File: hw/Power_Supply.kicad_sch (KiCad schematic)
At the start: 16 parts, among them U1 XC6206P332MR, U2 XC6206P332MR

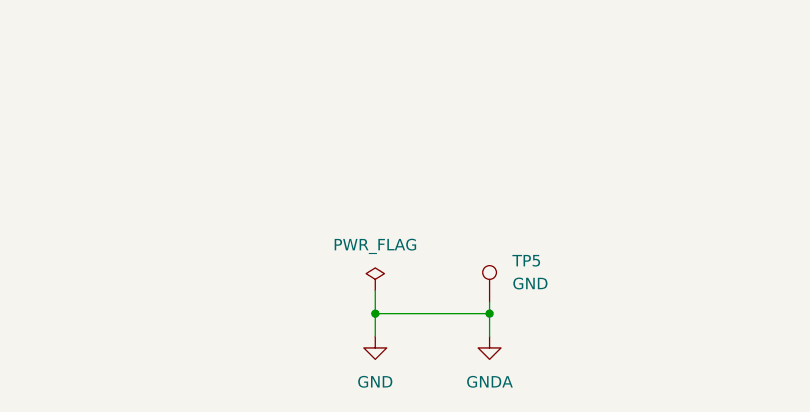
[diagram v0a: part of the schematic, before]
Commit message: added new pcb design, ERC errors not fixed yet
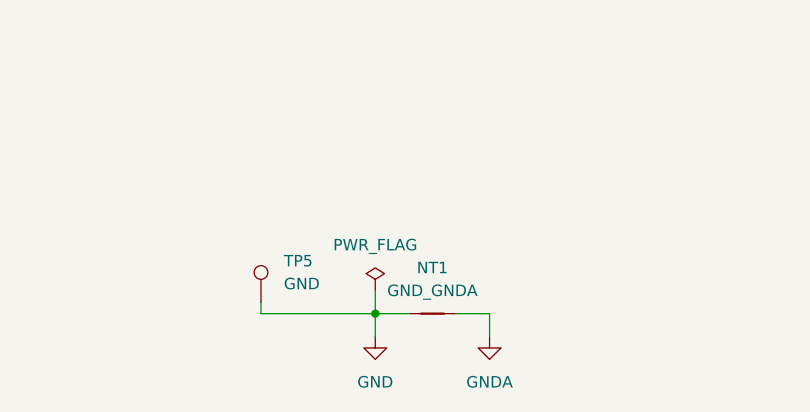
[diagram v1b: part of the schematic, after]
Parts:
- added NT1: GND_GNDA, NetTie:NetTie-2_SMD_Pad0.5mm, symbol Device:NetTie_2
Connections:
- net GND: now also NT1.1; no longer C6.2, C7.2, C8.2, U2.1 (GND)
- new net GNDA: C6.2, C7.2, C8.2, NT1.2, U2.1 (GND)
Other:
- moved on the sheet: TP5

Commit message: updates to hardware layer
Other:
- moved on the sheet: NT1, TP5
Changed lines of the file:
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@@
 	)
 	(junction
-		(at 149.86 176.53)
+		(at 83.82 163.83)
 		(diameter 0)
 		(color 0 0 0 0)
@@
 		(color 0 0 0 0)
 	)
+	(junction
+		(at 96.52 163.83)
+		(diameter 0)
+		(color 0 0 0 0)
+	)
 	(wire
 		(pts
@@
 	(wire
 		(pts
+			(xy 81.28 163.83) (xy 83.82 163.83)
+		)
+		(stroke
+			(width 0)
+			(type default)
+		)
+	)
+	(wire
+		(pts
 			(xy 203.2 91.44) (xy 203.2 88.9)
 		)
@@
 	(wire
 		(pts
-			(xy 149.86 173.99) (xy 149.86 176.53)
-		)
-		(stroke
-			(width 0)
-			(type default)
-		)
-	)
-	(wire
-		(pts
 			(xy 74.93 81.28) (xy 77.47 81.28)
 		)
@@
 	(wire
 		(pts
-			(xy 149.86 176.53) (xy 153.67 176.53)
+			(xy 83.82 163.83) (xy 87.63 163.83)
 		)
 		(stroke
@@
 	(wire
 		(pts
-			(xy 137.16 175.26) (xy 137.16 176.53)
+			(xy 83.82 162.56) (xy 83.82 163.83)
 		)
 		(stroke
@@
 	(wire
 		(pts
-			(xy 149.86 176.53) (xy 149.86 179.07)
+			(xy 83.82 163.83) (xy 83.82 166.37)
 		)
 		(stroke
@@
 	(wire
 		(pts
-			(xy 137.16 176.53) (xy 149.86 176.53)
-		)
-		(stroke
-			(width 0)
-			(type default)
-		)
-	)
-	(wire
-		(pts
 			(xy 135.89 101.6) (xy 148.59 101.6)
 		)
@@
 	(wire
 		(pts
+			(xy 99.06 163.83) (xy 96.52 163.83)
+		)
+		(stroke
+			(width 0)
+			(type default)
+		)
+	)
+	(wire
+		(pts
 			(xy 135.89 86.36) (xy 135.89 88.9)
 		)
@@
 	(wire
 		(pts
-			(xy 158.75 176.53) (xy 162.56 176.53)
+			(xy 92.71 163.83) (xy 96.52 163.83)
 		)
 		(stroke
@@
 	(wire
 		(pts
-			(xy 162.56 176.53) (xy 162.56 179.07)
+			(xy 96.52 163.83) (xy 96.52 166.37)
 		)
 		(stroke
@@
 	(symbol
 		(lib_id "power:PWR_FLAG")
-		(at 149.86 173.99 0)
-		(mirror y)
+		(at 99.06 163.83 270)
+		(mirror x)
+		(unit 1)
+		(exclude_from_sim no)
+		(in_bom yes)
+		(on_board yes)
+		(dnp no)
+		(fields_autoplaced yes)
+		(property "Reference" "#FLG01"
+			(at 100.965 163.83 0)
+			(effects
+				(font
+					(size 1.27 1.27)
+				)
+				(hide yes)
+			)
+		)
+		(property "Value" "PWR_FLAG"
+			(at 102.87 163.8299 90)
+			(effects
+				(font
+					(size 1.27 1.27)
+				)
+				(justify left)
+			)
+		)
+		(property "Footprint" ""
+			(at 99.06 163.83 0)
+			(effects
+				(font
+					(size 1.27 1.27)
+				)
+				(hide yes)
+			)
+		)
+		(property "Datasheet" "~"
+			(at 99.06 163.83 0)
+			(effects
+				(font
+					(size 1.27 1.27)
+				)
+				(hide yes)
+			)
+		)
+		(property "Description" "Special symbol for telling ERC where power comes from"
+			(at 99.06 163.83 0)
+			(effects
+				(font
+					(size 1.27 1.27)
+				)
+				(hide yes)
+			)
+		)
+		(pin "1"
+		)
+		(instances
+			(project "Expresso"
+				(path "/1e7cbae1-0003-4e27-ba62-2dd55b10f4f2/7b3e7736-e5d0-49f7-ac58-655fac733912"
+					(reference "#FLG01")
+					(unit 1)
+				)
+			)
+		)
+	)
+	(symbol
+		(lib_id "power:PWR_FLAG")
+		(at 81.28 163.83 90)
+		(mirror x)
 		(unit 1)
 		(exclude_from_sim no)
@@
 		(fields_autoplaced yes)
 		(property "Reference" "#FLG0101"
-			(at 149.86 172.085 0)
+			(at 79.375 163.83 0)
 			(effects
 				(font
@@
 		)
 		(property "Value" "PWR_FLAG"
-			(at 149.86 168.91 0)
-			(effects
-				(font
-					(size 1.27 1.27)
-				)
+			(at 77.47 163.8299 90)
+			(effects
+				(font
+					(size 1.27 1.27)
+				)
+				(justify left)
 			)
 		)
 		(property "Footprint" ""
-			(at 149.86 173.99 0)
+			(at 81.28 163.83 0)
 			(effects
 				(font
@@
 		)
 		(property "Datasheet" "~"
-			(at 149.86 173.99 0)
+			(at 81.28 163.83 0)
 			(effects
 				(font
@@
 		)
 		(property "Description" "Special symbol for telling ERC where power comes from"
-			(at 149.86 173.99 0)
+			(at 81.28 163.83 0)
 			(effects
 				(font
@@
 	(symbol
 		(lib_id "Connector:TestPoint")
-		(at 137.16 175.26 0)
+		(at 83.82 162.56 0)
 		(unit 1)
 		(exclude_from_sim no)
@@
 		(fields_autoplaced yes)
 		(property "Reference" "TP5"
-			(at 139.7 170.6879 0)
-			(effects
-				(font
-					(size 1.27 1.27)
-				)
-				(justify left)
+			(at 83.82 153.67 0)
+			(effects
+				(font
+					(size 1.27 1.27)
+				)
 			)
 		)
 		(property "Value" "GND"
-			(at 139.7 173.2279 0)
-			(effects
-				(font
-					(size 1.27 1.27)
-				)
-				(justify left)
+			(at 83.82 156.21 0)
+			(effects
+				(font
+					(size 1.27 1.27)
+				)
 			)
 		)
 		(property "Footprint" "TestPoint:TestPoint_Pad_D2.0mm"
-			(at 142.24 175.26 0)
+			(at 88.9 162.56 0)
 			(effects
 				(font
@@
 		)
 		(property "Datasheet" "~"
-			(at 142.24 175.26 0)
+			(at 88.9 162.56 0)
 			(effects
 				(font
@@
 		)
 		(property "Description" "test point"
-			(at 137.16 175.26 0)
+			(at 83.82 162.56 0)
 			(effects
 				(font
@@
 	(symbol
 		(lib_id "power:GND")
-		(at 149.86 179.07 0)
+		(at 83.82 166.37 0)
 		(unit 1)
 		(exclude_from_sim no)
@@
 		(fields_autoplaced yes)
 		(property "Reference" "#PWR0101"
-			(at 149.86 185.42 0)
+			(at 83.82 172.72 0)
 			(effects
 				(font
@@
 		)
 		(property "Value" "GND"
-			(at 149.86 184.15 0)
+			(at 83.82 171.45 0)
 			(effects
 				(font
@@
 		)
 		(property "Footprint" ""
-			(at 149.86 179.07 0)
+			(at 83.82 166.37 0)
 			(effects
 				(font
@@
 		)
 		(property "Datasheet" ""
-			(at 149.86 179.07 0)
+			(at 83.82 166.37 0)
 			(effects
 				(font
@@
 		)
 		(property "Description" "Power symbol creates a global label with name \"GND\" , ground"
-			(at 149.86 179.07 0)
+			(at 83.82 166.37 0)
 			(effects
 				(font
@@
 	(symbol
 		(lib_id "power:GNDA")
-		(at 162.56 179.07 0)
+		(at 96.52 166.37 0)
 		(unit 1)
 		(exclude_from_sim no)
@@
 		(fields_autoplaced yes)
 		(property "Reference" "#PWR0102"
-			(at 162.56 185.42 0)
+			(at 96.52 172.72 0)
 			(effects
 				(font
@@
 		)
 		(property "Value" "GNDA"
-			(at 162.56 184.15 0)
+			(at 96.52 171.45 0)
 			(effects
 				(font
@@
 		)
 		(property "Footprint" ""
-			(at 162.56 179.07 0)
+			(at 96.52 166.37 0)
 			(effects
 				(font
@@
 		)
 		(property "Datasheet" ""
-			(at 162.56 179.07 0)
+			(at 96.52 166.37 0)
 			(effects
 				(font
@@
 		)
 		(property "Description" "Power symbol creates a global label with name \"GNDA\" , analog ground"
-			(at 162.56 179.07 0)
+			(at 96.52 166.37 0)
 			(effects
 				(font
@@
 	(symbol
 		(lib_id "Device:NetTie_2")
-		(at 156.21 176.53 0)
+		(at 90.17 163.83 0)
 		(unit 1)
 		(exclude_from_sim no)
@@
 		(dnp no)
 		(property "Reference" "NT1"
-			(at 156.21 171.45 0)
+			(at 90.17 158.75 0)
 			(effects
 				(font
@@
 		)
 		(property "Value" "GND_GNDA"
-			(at 156.21 173.99 0)
+			(at 90.17 161.29 0)
 			(effects
 				(font
@@
 		)
 		(property "Footprint" "NetTie:NetTie-2_SMD_Pad0.5mm"
-			(at 156.21 176.53 0)
+			(at 90.17 163.83 0)
 			(effects
 				(font
@@
 		)
 		(property "Datasheet" "~"
-			(at 156.21 176.53 0)
+			(at 90.17 163.83 0)
 			(effects
 				(font
@@
 		)
 		(property "Description" "Net tie, 2 pins"
-			(at 156.21 176.53 0)
-			(effects
-				(font
+			(at 90.17 163.83 0)
+			(effects
+				(font
